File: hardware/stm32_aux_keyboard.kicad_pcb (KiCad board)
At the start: 2 copper layers, 95 x 95 mm, 188 parts, among them J1 I2C_HEADER,2.54, J2 WS2812_HEADER, J3 BUZZER_HEADER, J4 ROT_ENC_HEADER, J5 SWD_SWD, J6 SWD_SWD, J7 ROT_ENC_HEADER, J8 I2C_HEADER,2.54, Q1 SS9013_J3, SW1 USR_BTN_1, SW10 KEY22, SW11 KEY23, SW12 KEY31, SW13 KEY32, SW14 KEY33, SW18 ROT1, SW19 SW_RESET,2_leg,SMD, SW2 USR_BTN_2, SW3 USR_BTN_3, SW5 ROT2, SW6 KEY11, SW7 KEY12, SW8 KEY13, SW9 KEY21, U1 SSD1306-OLED-I2C, U10 STM32F103C8T6, U2 AMS1117-3.3, U3 74AHCT1G125, U4 USB, U5 USBLC6-2SC6_SOT23-6, U6 STM32F103C8T6_rect, U7 SWD, U8 AMS1117-3.3, U9 USBLC6-2SC6_SOT23-6, Y1 O_8M, Y2 O8M, Y3 O32.768K

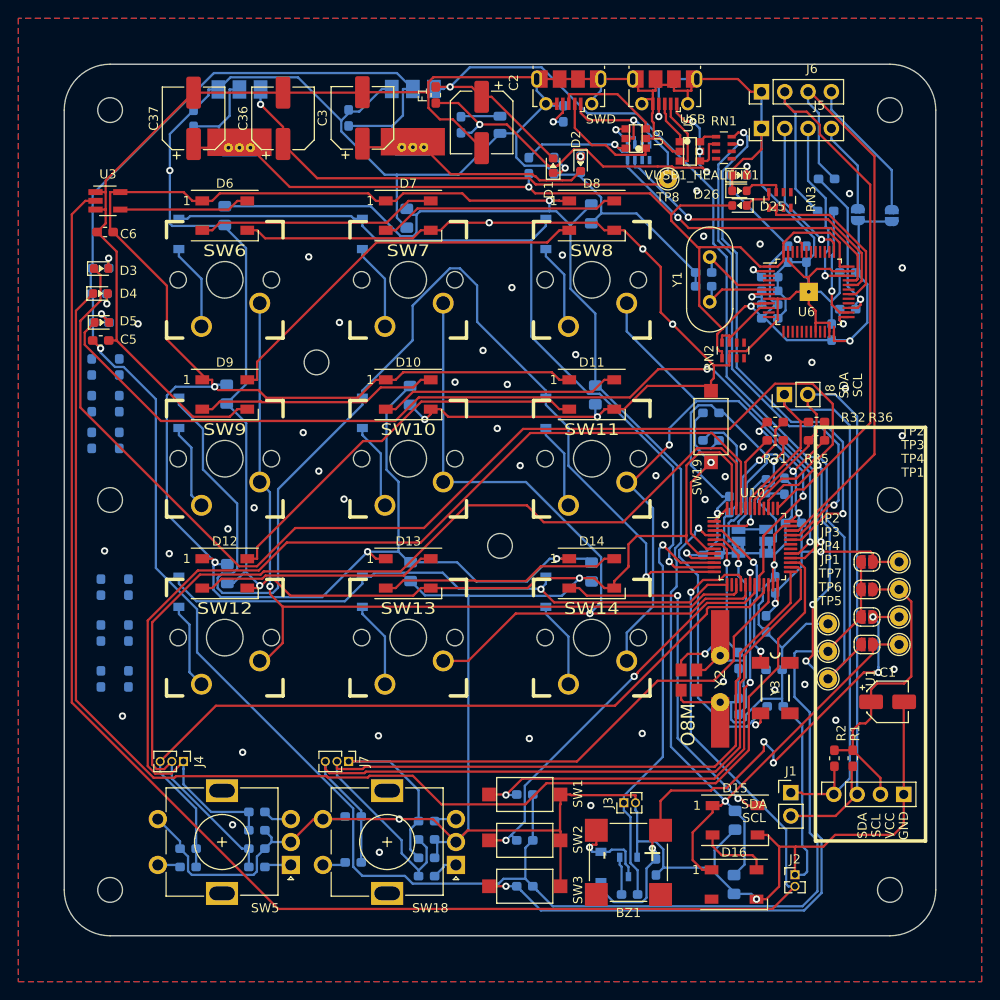
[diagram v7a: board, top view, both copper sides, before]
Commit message: update for tidy tracks,
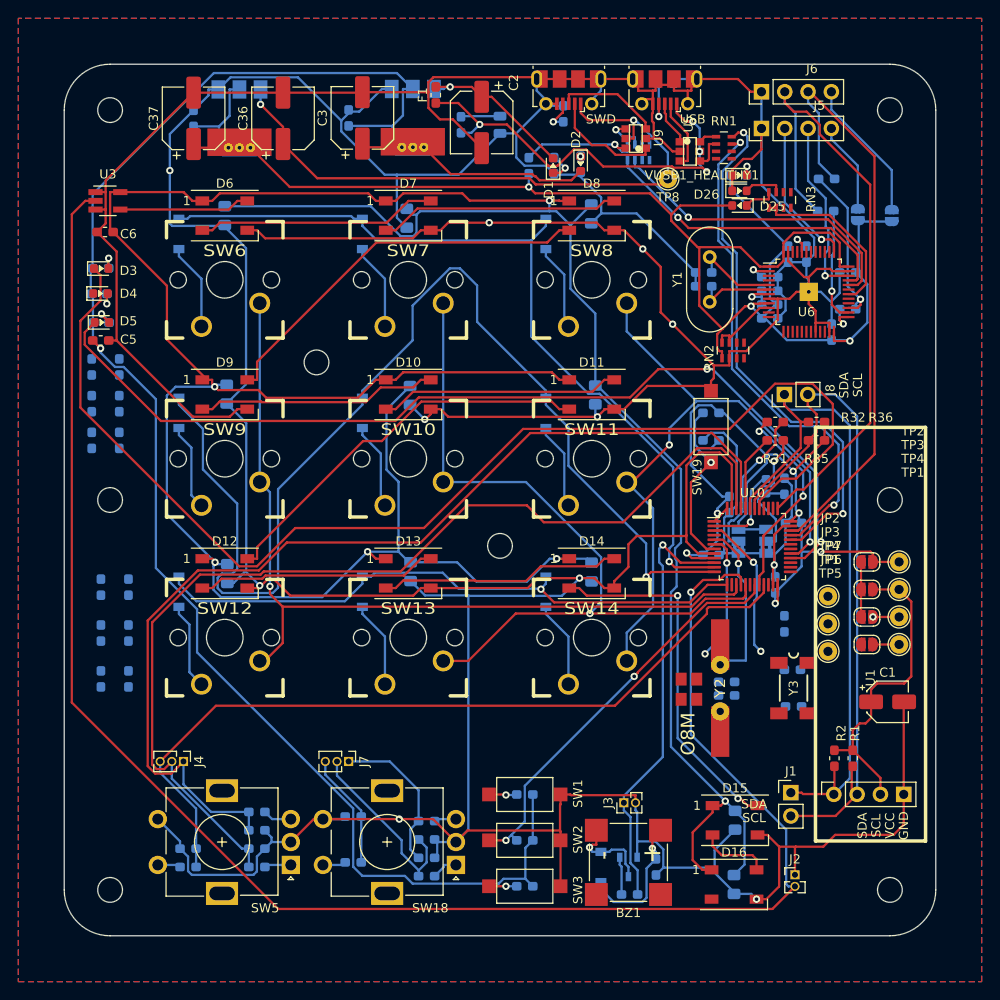
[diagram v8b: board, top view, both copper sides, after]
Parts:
- moved C48 4.02 mm to (92.2, 88.8), turned to 0 degrees
- moved TP5 3.00 mm to (103.2, 84.0)
- moved TP6 3.00 mm to (103.2, 81.0)
- moved TP7 3.00 mm to (103.2, 78.0)
- moved C47 2.97 mm to (92.2, 87.3), turned to 0 degrees
- moved C42 2.00 mm to (98.5, 81.0)
- moved C49 2.00 mm to (99.4, 86.0)
- moved C50 2.00 mm to (99.5, 90.0)
- moved Y3 2.00 mm to (99.5, 88.0)
- moved Y2 1.00 mm to (91.5, 88.0)
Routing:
- net /status_display/USR_LED_2: track 150.1 -> 0.00 mm
- net +5V: track 118.9 -> 18.0 mm
- net /stm32_core/USR_BTN3: track 95.0 -> 3.03 mm, vias 4 -> 1
- net /stm32_core/ROT_ENC_SW2: track 83.3 -> 12.6 mm
- net +3V3: track 273.1 -> 204.5 mm
- net /rot_enc/B: track 87.1 -> 20.3 mm
- net GND: track 886.9 -> 822.2 mm, vias 56 -> 11
- net /rot_enc/A: track 73.4 -> 17.0 mm
- net /stm32_core/USR_BTN1: track 52.0 -> 3.07 mm, vias 3 -> 1
- net Vbuzzer: track 59.9 -> 17.7 mm, vias 5 -> 2
- net /stm32_core/OSC32K_N: track 34.1 -> 0.00 mm, vias 2 -> 0
- net VCC: track 387.6 -> 363.8 mm
- net /stm32_core/OSC_P: track 30.0 -> 19.7 mm
- net /stm32_core/OSC_N: track 20.3 -> 14.6 mm
- net /stm32_core/OSC32K_P: track 19.5 -> 16.0 mm
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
